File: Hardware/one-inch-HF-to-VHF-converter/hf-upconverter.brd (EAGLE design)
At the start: 25.1 x 25.4 mm, 14 parts, among them IC1 74VHC4053, T1 PT61018PEL

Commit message: Small schematic symbol change in HF upconverter
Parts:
- L1: device rcl:R1206 -> L1206:R1206
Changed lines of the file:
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@@
 <element name="IC1" library="40xx" package="SO16" value="74VHC4053" x="20.0025" y="12.7" rot="R270"/>
 <element name="JP1" library="SparkFun-Connectors" package="USB-A-SMT-MALE" value="USBA-SMD-MALE" x="12.7" y="25.4"/>
-<element name="L1" library="rcl" package="R1206" value="220nH" x="12.3825" y="5.08" rot="R180"/>
+<element name="L1" library="L1206" package="R1206" value="220nH" x="12.3825" y="5.08" rot="R180"/>
 <element name="OS1" library="IQD-Frequency-Products" package="7.2X5.2-4-PAD" value="50MHz" x="6.0325" y="15.24" rot="MR180"/>
 <element name="SMA1" library="SparkFun-Connectors" package="SMA-EDGE" value="ANT" x="22.86" y="0.9525" rot="MR90"/>

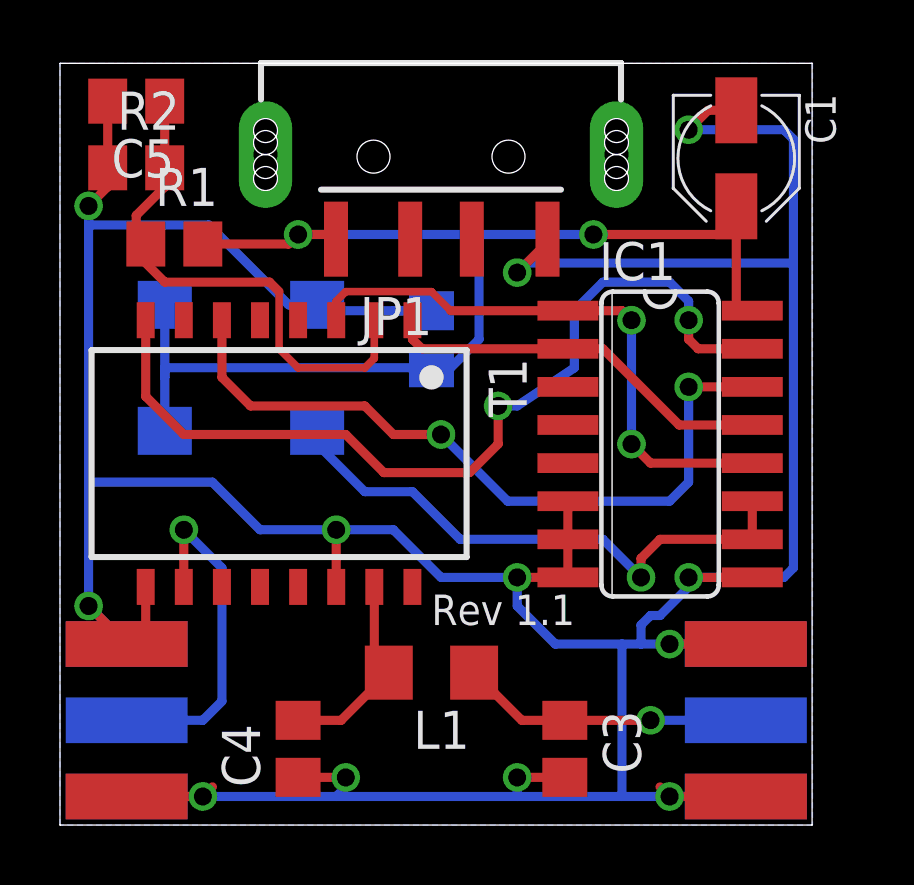
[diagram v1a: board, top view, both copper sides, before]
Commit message: Updated PCB to v1.2, with SMA connector centre pins on top of the board.
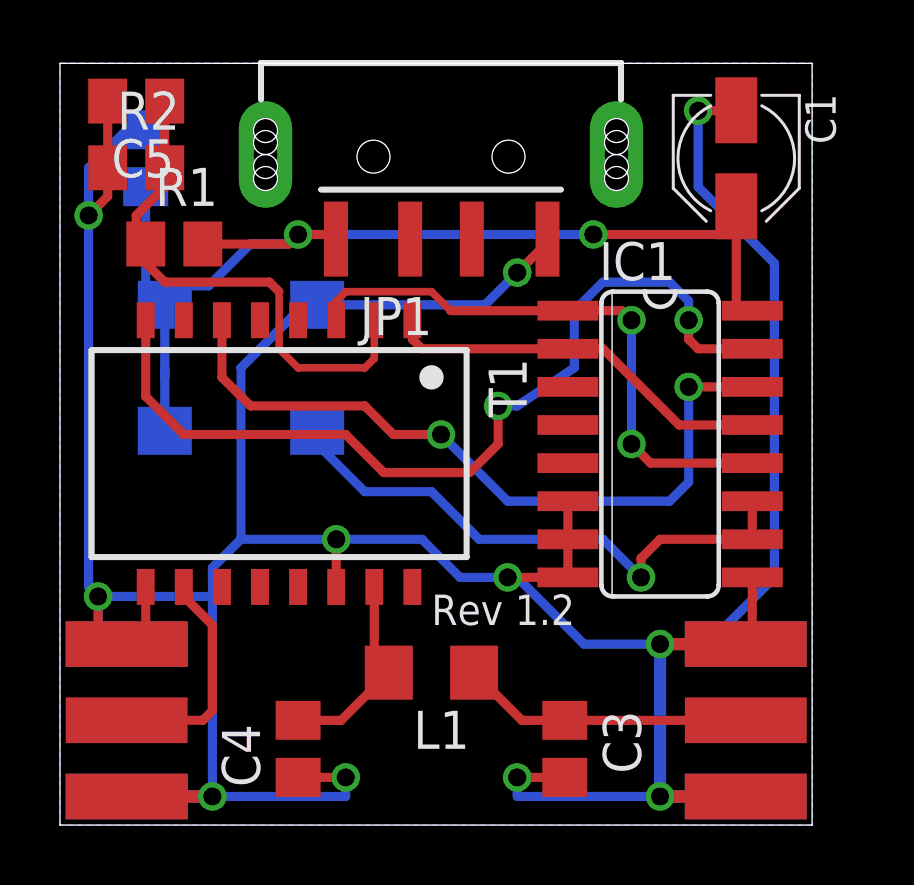
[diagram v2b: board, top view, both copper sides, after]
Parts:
- moved C2 11.3 mm to (2.86, 22.2)
- flipped SMA1 to the top
- flipped SMA2 to the top
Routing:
- net GND: track 148.7 -> 139.6 mm, vias 12 -> 11
- net VCC: track 42.2 -> 37.9 mm
- net N$14: track 11.6 -> 7.51 mm, vias 1 -> 0
- net N$5: vias 1 -> 0
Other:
- board text added: "Rev 1.2"
- board text removed: "Rev 1.1"
